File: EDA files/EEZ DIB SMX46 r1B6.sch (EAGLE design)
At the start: 143 parts, among them IC1 STM32F030C6T6, IC2 74HC1G126GW,125, IC3 M24C32-WMN6P, IC4 LP2985-33DBVR, IC5 74HC2G04GW,125, IC6 OPA2990IDR, K1 FTR-C1GA012G-B05, K10 FTR-C1GA012G-B05, K11 FTR-C1GA012G-B05, K12 FTR-C1GA012G-B05, K13 FTR-C1GA012G-B05, K14 FTR-C1GA012G-B05, K15 FTR-C1GA012G-B05, K16 FTR-C1GA012G-B05, K17 FTR-C1GA012G-B05, K18 FTR-C1GA012G-B05, K19 RT424005, K2 FTR-C1GA012G-B05, K20 FTR-C1GA012G-B05, K21 FTR-C1GA012G-B05, K22 FTR-C1GA012G-B05, K23 FTR-C1GA012G-B05, K24 FTR-C1GA012G-B05, K25 FTR-C1GA012G-B05, K3 FTR-C1GA012G-B05, K4 FTR-C1GA012G-B05, K5 FTR-C1GA012G-B05, K6 FTR-C1GA012G-B05, K7 FTR-C1GA012G-B05, K8 FTR-C1GA012G-B05, K9 FTR-C1GA012G-B05, Q1 2N7002, Q10 2N7002, Q11 2N7002, Q12 2N7002, Q13 2N7002, Q14 2N7002, Q15 2N7002, Q16 2N7002, Q17 2N7002, Q18 2N7002, Q19 2N7002, Q2 2N7002, Q20 2N7002, Q21 2N7002, Q22 2N7002, Q23 2N7002, Q24 2N7002, Q25 2N7002, Q3 2N7002, Q4 2N7002, Q5 2N7002, Q6 2N7002, Q7 2N7002, Q8 2N7002, Q9 2N7002, X1 N.C., X2 77317-104-28LF, X3 691327310016, X4 691327310016, X6 DS1014-10RF1B, X7 DS1014-10RF1B

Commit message: ADIB ID=001
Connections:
- new net N$10: X6-10.1, X6-7.1
- new net N$11: X7-10.1, X7-7.1
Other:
- note added: "ADIB1_ID=001"
- note added: "ADIB2_ID=001"
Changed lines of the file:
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@@
 <text x="7.62" y="88.9" size="1.778" layer="97" rot="MR180">ADIB connectors</text>
 <wire x1="142.24" y1="91.44" x2="5.08" y2="91.44" width="0.1524" layer="97" style="shortdash"/>
+<text x="27.94" y="66.675" size="1.4224" layer="103">ADIB1_ID=001</text>
+<text x="81.28" y="66.675" size="1.4224" layer="103">ADIB2_ID=001</text>
 </plain>
 <instances>
@@
 </segment>
 </net>
+<net name="N$10" class="0">
+<segment>
+<pinref part="X6" gate="-7" pin="1"/>
+<wire x1="30.48" y1="73.66" x2="27.94" y2="73.66" width="0.1524" layer="91"/>
+<wire x1="27.94" y1="73.66" x2="27.94" y2="68.58" width="0.1524" layer="91"/>
+<wire x1="27.94" y1="68.58" x2="58.42" y2="68.58" width="0.1524" layer="91"/>
+<wire x1="58.42" y1="68.58" x2="58.42" y2="71.12" width="0.1524" layer="91"/>
+<pinref part="X6" gate="-10" pin="1"/>
+<wire x1="58.42" y1="71.12" x2="55.88" y2="71.12" width="0.1524" layer="91"/>
+</segment>
+</net>
+<net name="N$11" class="0">
+<segment>
+<pinref part="X7" gate="-7" pin="1"/>
+<wire x1="83.82" y1="73.66" x2="81.28" y2="73.66" width="0.1524" layer="91"/>
+<wire x1="81.28" y1="73.66" x2="81.28" y2="68.58" width="0.1524" layer="91"/>
+<wire x1="81.28" y1="68.58" x2="111.76" y2="68.58" width="0.1524" layer="91"/>
+<wire x1="111.76" y1="68.58" x2="111.76" y2="71.12" width="0.1524" layer="91"/>
+<pinref part="X7" gate="-10" pin="1"/>
+<wire x1="111.76" y1="71.12" x2="109.22" y2="71.12" width="0.1524" layer="91"/>
+</segment>
+</net>

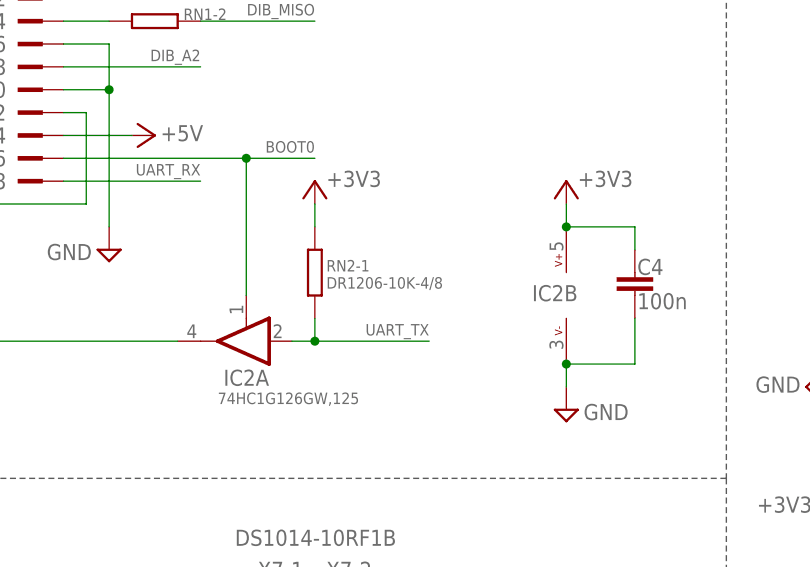
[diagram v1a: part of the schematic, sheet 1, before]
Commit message: RN2 value update
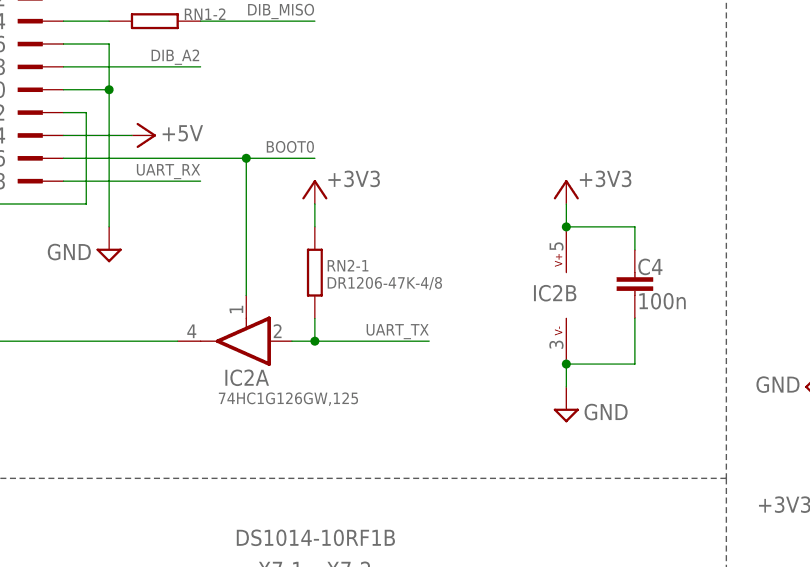
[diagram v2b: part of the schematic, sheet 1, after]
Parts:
- RN2: value DR1206-10K-4/8 -> DR1206-47K-4/8
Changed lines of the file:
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@@
 <part name="SUPPLY7" library="supply2" deviceset="GND" device=""/>
 <part name="C9" library="rcl" deviceset="C-EU" device="C0805" value="2u2"/>
-<part name="RN2" library="EEZ_Lib1" deviceset="R_ARRAY4" device="" value="DR1206-10K-4/8"/>
+<part name="RN2" library="EEZ_Lib1" deviceset="R_ARRAY4" device="" value="DR1206-47K-4/8"/>
 <part name="+3V32" library="supply1" deviceset="+3V3" device=""/>
 <part name="+3V38" library="supply1" deviceset="+3V3" device=""/>

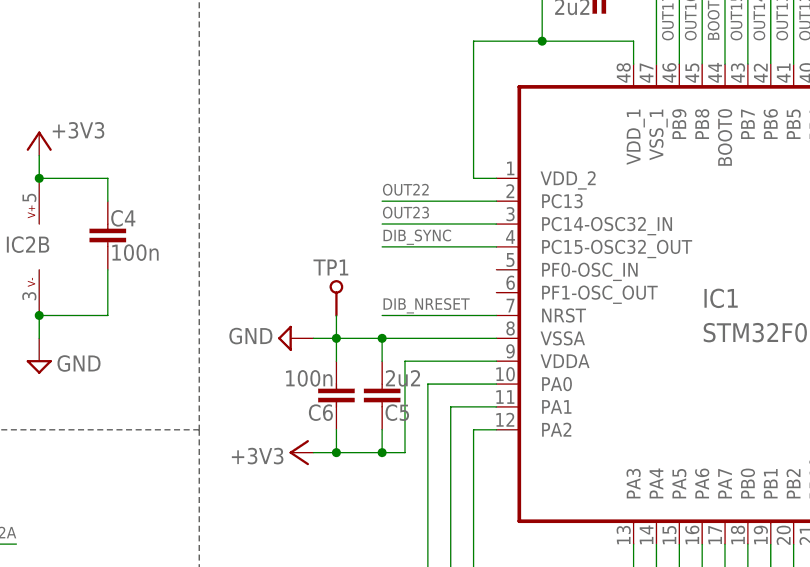
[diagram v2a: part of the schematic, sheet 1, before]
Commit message: PCB ID added
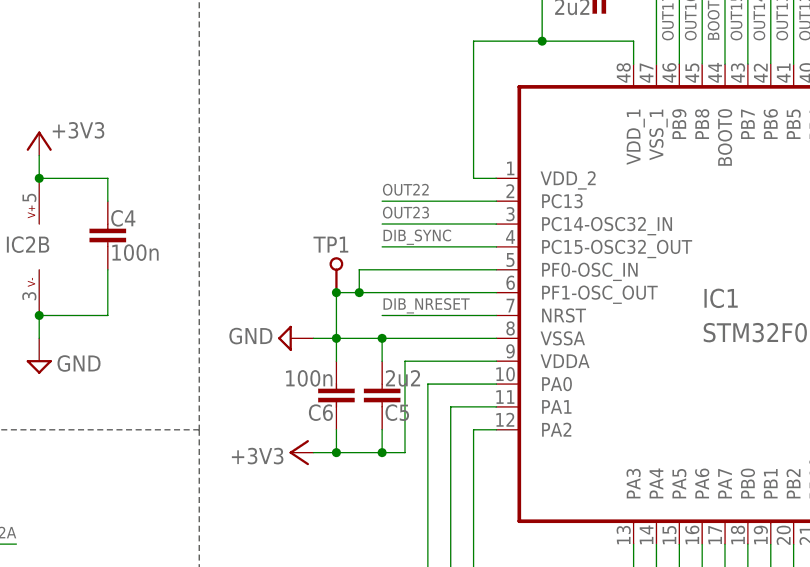
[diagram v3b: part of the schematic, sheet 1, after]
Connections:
- net GND: now also IC1.PF0-OSC_IN, IC1.PF1-OSC_OUT
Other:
- note added: "PCB_ID0"
- note added: "PCB_ID1"
- note added: "PCB_ID=0"
- moved on the sheet: TP1
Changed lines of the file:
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@@
 <text x="27.94" y="66.675" size="1.4224" layer="103">ADIB1_ID=001</text>
 <text x="81.28" y="66.675" size="1.4224" layer="103">ADIB2_ID=001</text>
+<text x="162.56" y="107.315" size="1.27" layer="103">PCB_ID1</text>
+<text x="162.56" y="109.855" size="1.27" layer="103">PCB_ID0</text>
+<text x="144.78" y="109.855" size="1.27" layer="103">PCB_ID=0</text>
 </plain>
 <instances>
@@
 <attribute name="NAME" x="178.308" y="165.862" size="1.524" layer="95" rot="MR180"/>
 </instance>
-<instance part="TP1" gate="G$1" x="157.48" y="106.68" smashed="yes" rot="R90">
-<attribute name="NAME" x="154.94" y="108.585" size="1.778" layer="95"/>
-<attribute name="VALUE" x="160.02" y="106.68" size="1.778" layer="96" rot="R90"/>
+<instance part="TP1" gate="G$1" x="157.48" y="109.22" smashed="yes" rot="R90">
+<attribute name="NAME" x="154.94" y="111.125" size="1.778" layer="95"/>
+<attribute name="VALUE" x="160.02" y="109.22" size="1.778" layer="96" rot="R90"/>
 </instance>
 <instance part="JP1" gate="G$1" x="246.38" y="86.36" smashed="yes" rot="MR90">
@@
 <junction x="157.48" y="101.6"/>
 <pinref part="TP1" gate="G$1" pin="P$1"/>
-<wire x1="157.48" y1="104.14" x2="157.48" y2="101.6" width="0.1524" layer="91"/>
+<wire x1="157.48" y1="106.68" x2="157.48" y2="101.6" width="0.1524" layer="91"/>
+<pinref part="IC1" gate="G$1" pin="PF1-OSC_OUT"/>
+<wire x1="175.26" y1="106.68" x2="160.02" y2="106.68" width="0.1524" layer="91"/>
+<junction x="157.48" y="106.68"/>
+<pinref part="IC1" gate="G$1" pin="PF0-OSC_IN"/>
+<wire x1="160.02" y1="106.68" x2="157.48" y2="106.68" width="0.1524" layer="91"/>
+<wire x1="175.26" y1="109.22" x2="160.02" y2="109.22" width="0.1524" layer="91"/>
+<wire x1="160.02" y1="109.22" x2="160.02" y2="106.68" width="0.1524" layer="91"/>
+<junction x="160.02" y="106.68"/>
 </segment>
 </net>
